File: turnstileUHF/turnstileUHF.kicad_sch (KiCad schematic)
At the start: 57 parts, among them J1 Conn_Coaxial, J2 Conn_Coaxial, J3 Conn_Coaxial, J4 Conn_Coaxial, Q1 2N7002, Q2 2N7002, Q3 2N7002, Q4 2N7002, Q5 AO3401A, Q6 AO3401A, Q7 AO3401A, Q8 2N7002, SW1 SW_DIP_x04

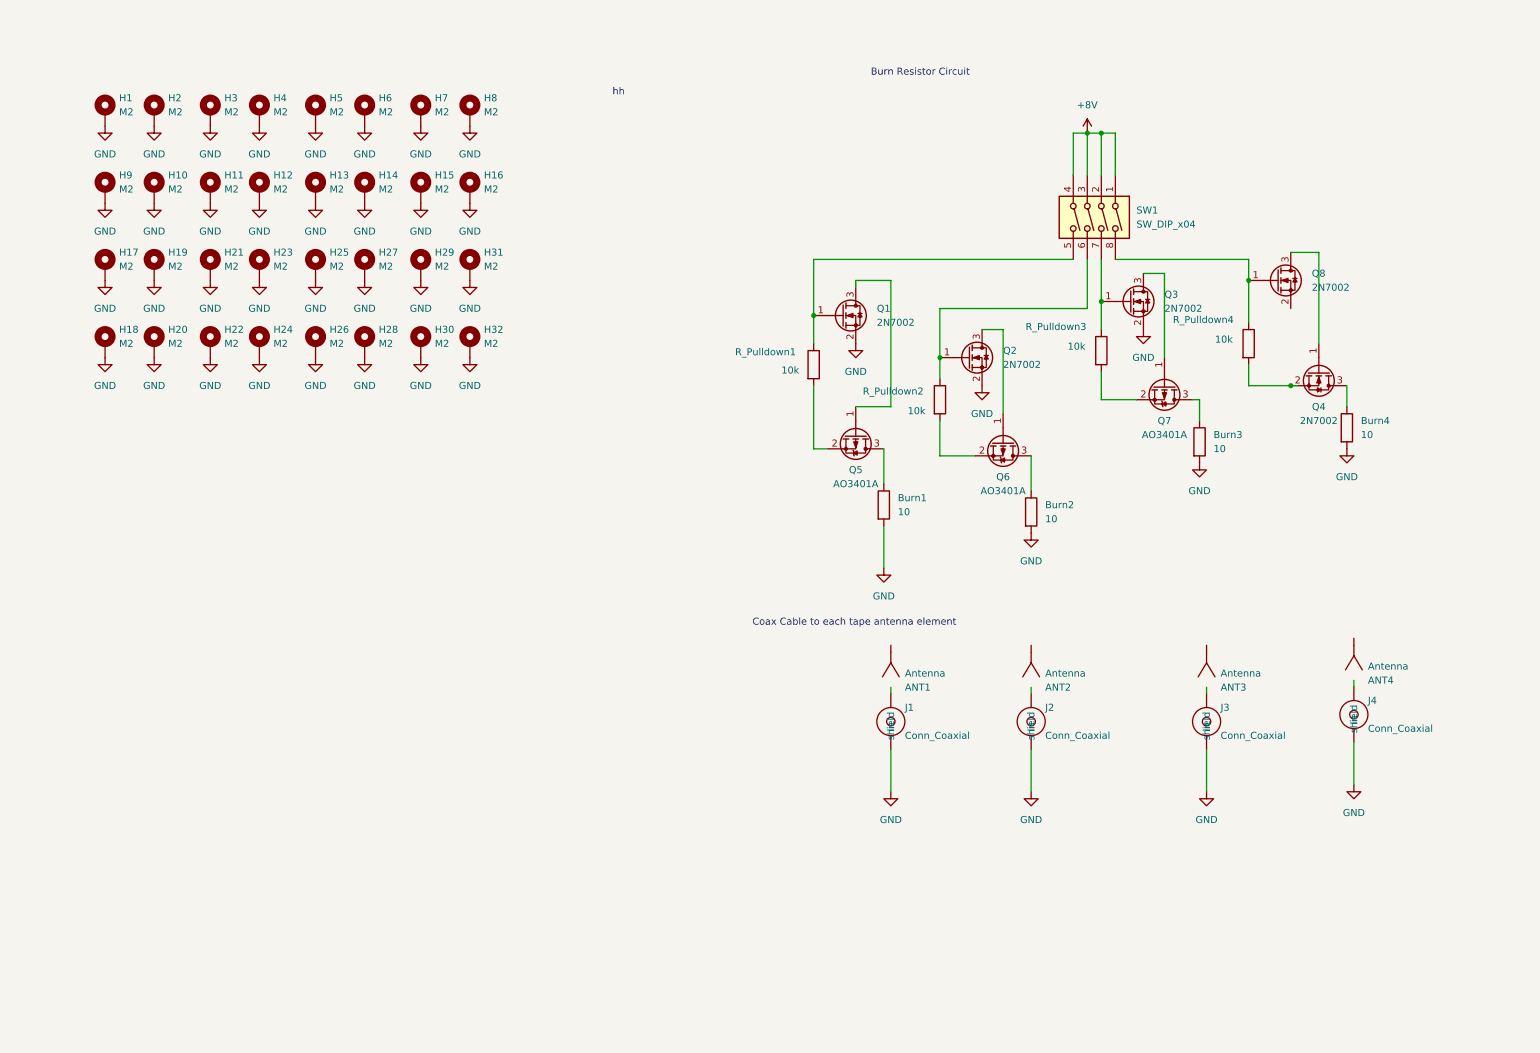
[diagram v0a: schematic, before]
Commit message: Added new 74HCT238D decoder and re-organisation of schematic
Added the 74HCT238D decoder and I also re-organised the schematic.
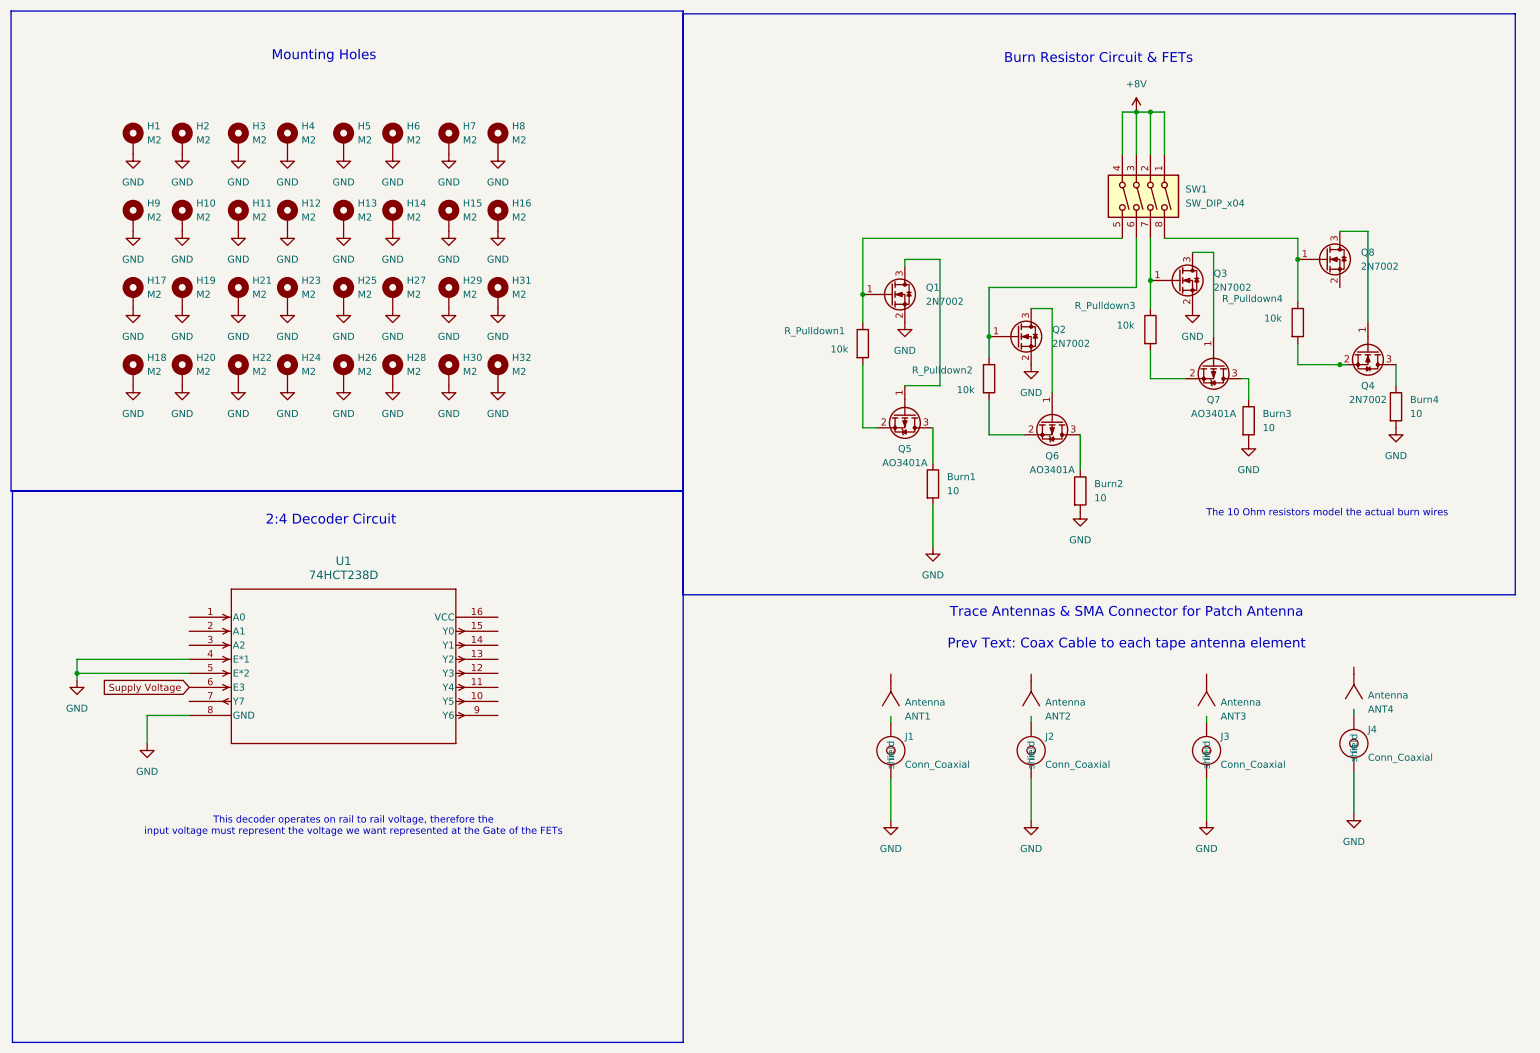
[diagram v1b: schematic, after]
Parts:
- added U1: 74HCT238D, inspireFly:SOT109-1_NXP, symbol inspireFly:74HCT238D
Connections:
- net GND: now also U1.4 (E*1), U1.5 (E*2), U1.8 (GND)
- new net Supply Voltage: U1.6 (E3)
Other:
- note added: "2:4 Decoder Circuit"
- note added: "Burn Resistor Circuit & FETs"
- note added: "Mounting Holes"
- note added: "The 10 Ohm resistors model the actual burn wires"
- note added: "This decoder operates on rail to rail voltage, therefore the input voltage must represent the voltage we want represented at the Gate of the FETs"
- note added: "Trace Antennas & SMA Connector for Patch Antenna Prev Text: Coax Cable to each tape antenna element"
- note removed: "Burn Resistor Circuit"
- note removed: "Coax Cable to each tape antenna element"
- note removed: "hh"
- moved on the sheet: ANT1, ANT2, ANT3, ANT4, Burn1, Burn2, Burn3, Burn4, H1, H10, H11, H12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

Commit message: Further changes made. Added SMA connector & Changed the placement of the trace antennas
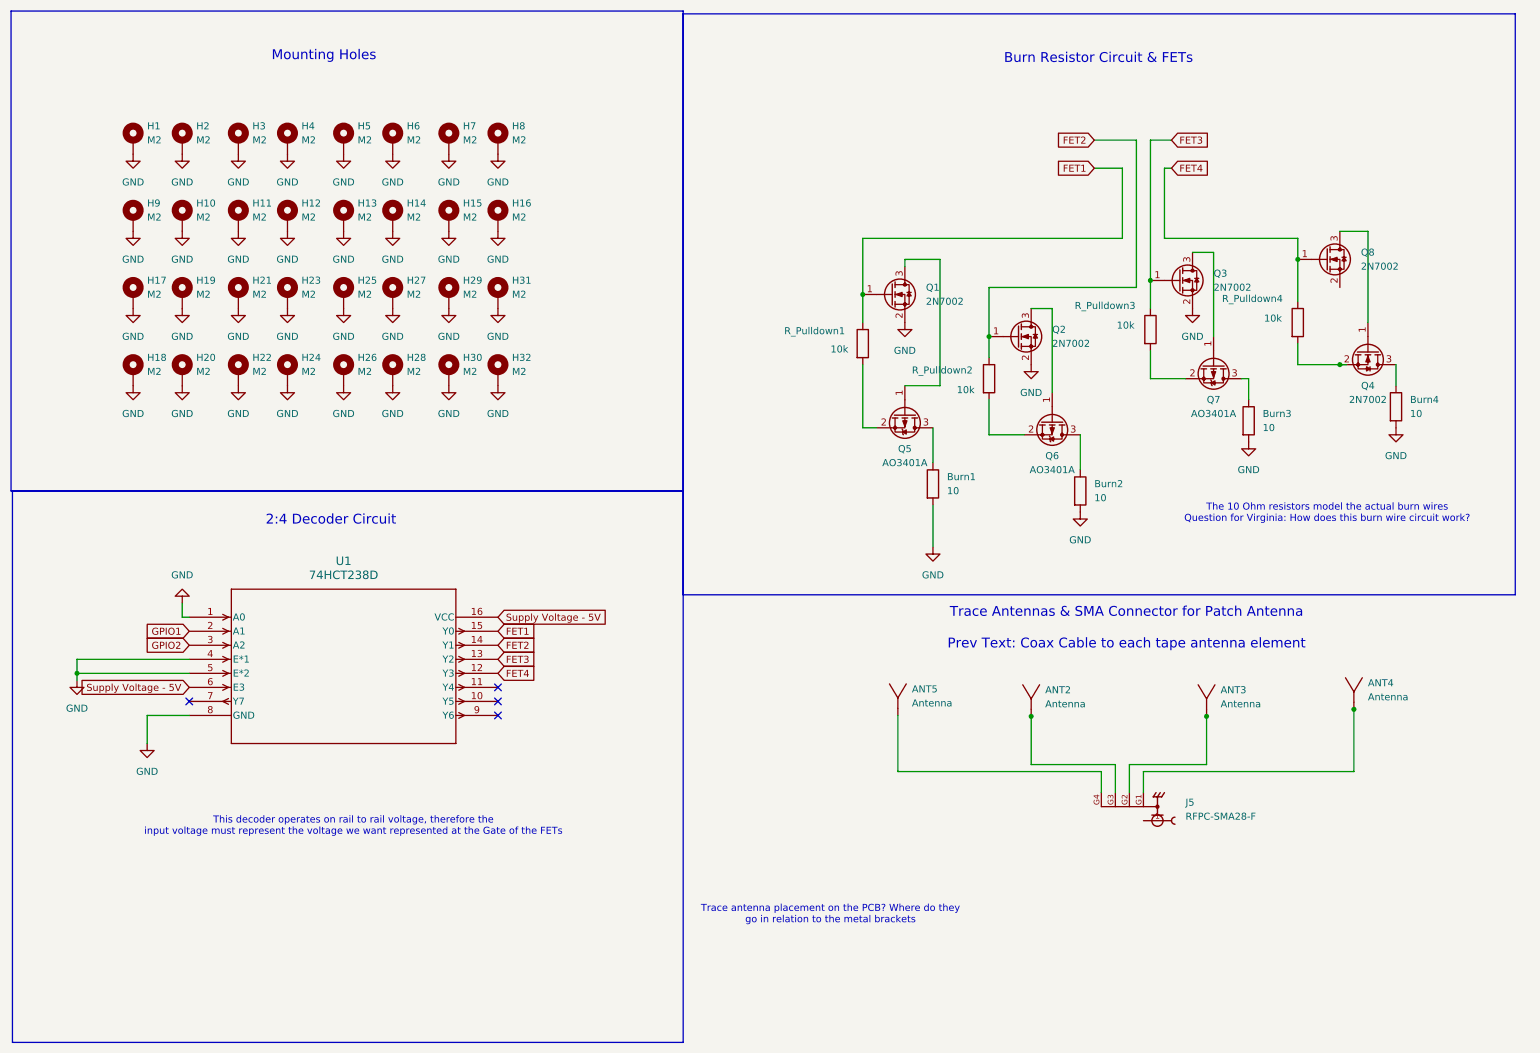
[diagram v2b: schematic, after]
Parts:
- removed ANT1: Antenna, symbol Device:Antenna
- removed J1, J2, J3, J4: Conn_Coaxial, Connector_Coaxial:U.FL_Hirose_U.FL-R-SMT-1_Vertical, symbol Connector:Conn_Coaxial
- removed SW1: SW_DIP_x04, Button_Switch_SMD:SW_DIP_SPSTx04_Slide_6.7x11.72mm_W8.61mm_P2.54mm_LowProfile, symbol Switch:SW_DIP_x04
- added ANT5: Antenna, symbol Device:Antenna
- added J5: RFPC-SMA28-F, inspireFly:GRADCONN_RFPC-SMA28-F, symbol inspireFly:RFPC-SMA28-F
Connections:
- net Supply Voltage is gone; now on net Supply Voltage - 5V: U1.6 (E3)
- net GND: now also U1.1 (A0)
- net FET1: now reaches Q1.1 (G), R_Pulldown1.1
- net FET1: now also U1.15 (Y0)
- net at ANT2.1: now also J5.G3
- net FET3: now reaches Q3.1 (G), R_Pulldown3.1
- net FET3: now also U1.13 (Y2)
- net FET2: now reaches Q2.1 (G), R_Pulldown2.1
- net FET2: now also U1.14 (Y1)
- net at ANT4.1: now also J5.G1
- net FET4: now reaches U1.12 (Y3)
- net FET4: now also Q8.1 (G), R_Pulldown4.1
- net Supply Voltage - 5V: now reaches U1.16 (VCC)
- net GPIO1: now reaches U1.2 (A1)
- net GPIO2: now reaches U1.3 (A2)
- net at ANT3.1: now also J5.G2
- new net: ANT5.1, J5.G4
- no-connect marks 0 -> 4
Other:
- note added: "The 10 Ohm resistors model the actual burn wires Question for Virginia: How does this burn wire circuit work?"
- note added: "Trace antenna placement on the PCB? Where do they go in relation to the metal brackets"
- note removed: "The 10 Ohm resistors model the actual burn wires"
- moved on the sheet: ANT2, ANT3, ANT4

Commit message: Meeting changes 09-25-2026
Changes made to the schematic, ready to be routed
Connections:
- net GND: now also J5.G1, J5.G2, J5.G3, J5.G4
- net at J5.1: now also ANT2.1, ANT3.1, ANT4.1, ANT5.1
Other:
- note added: "The 10 Ohm resistors model the actual burn wires"
- note removed: "The 10 Ohm resistors model the actual burn wires Question for Virginia: How does this burn wire circuit work?"
- moved on the sheet: J5

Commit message: fixed missing antenna
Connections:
- net FET3: now also Q8.1 (G), R_Pulldown4.1; no longer Q3.1 (G), R_Pulldown3.1
- net FET4: now also Q3.1 (G), R_Pulldown3.1, U1.9 (Y6); no longer Q8.1 (G), R_Pulldown4.1, U1.12 (Y3)
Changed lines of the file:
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@@
+	)
+	(no_connect
+		(at 100.33 132.08)
 	)
 	(no_connect
@@
 	(no_connect
 		(at 100.33 134.62)
-	)
-	(no_connect
-		(at 100.33 139.7)
 	)
 	(wire
@@
 	(global_label "FET4"
 		(shape input)
-		(at 100.33 132.08 0)
+		(at 100.33 139.7 0)
 		(fields_autoplaced yes)
 		(effects
@@
 		)
 		(property "Intersheetrefs" "${INTERSHEET_REFS}"
-			(at 107.7299 132.08 0)
+			(at 107.7299 139.7 0)
 			(hide yes)
 			(show_name no)
@@
 		)
 	)
-	(global_label "FET4"
+	(global_label "FET3"
 		(shape input)
 		(at 222.25 40.64 0)
@@
 		)
 	)
-	(global_label "FET3"
+	(global_label "FET4"
 		(shape input)
 		(at 222.25 35.56 0)
